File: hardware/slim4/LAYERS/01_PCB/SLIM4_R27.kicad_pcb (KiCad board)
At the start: 6 copper layers, 99.2 x 125 mm, 167 parts, among them J1 FH12A-40S-0.5SH(55), J2 USB4105-GF-A-120, J3 S2B-PH-SM4-TB(LF)(SN), J4 53261-0271, J5 53261-0271, Q1 2N7002, Q2 AO3401A, SW1 D2LS-21, SW2 D2LS-21, SW3 D2LS-21, SW4 D2LS-21, SW5 B3U-1000P, SW6 B3U-1000P, SW7 B3U-1000P, U1 ESP32-P4NRW32X, U10 BQ24074RGTR, U11 TPD2EUSB30DRTR, U12 TPD2EUSB30DRTR, U13 TUSB320LAIRWBR, U14 TPS3808G33DBVR, U2 W25Q512JVEIQ TR, U3 TLV62569DBVR, U4 TPS63070RNMR, U5 TLV75518PDBVR, U6 ME6211C30M5G-N, U7 TPS61165DBVR, U8 MAX98357AETE+T, U9 MAX98357AETE+T, Y1 L327S400H11L

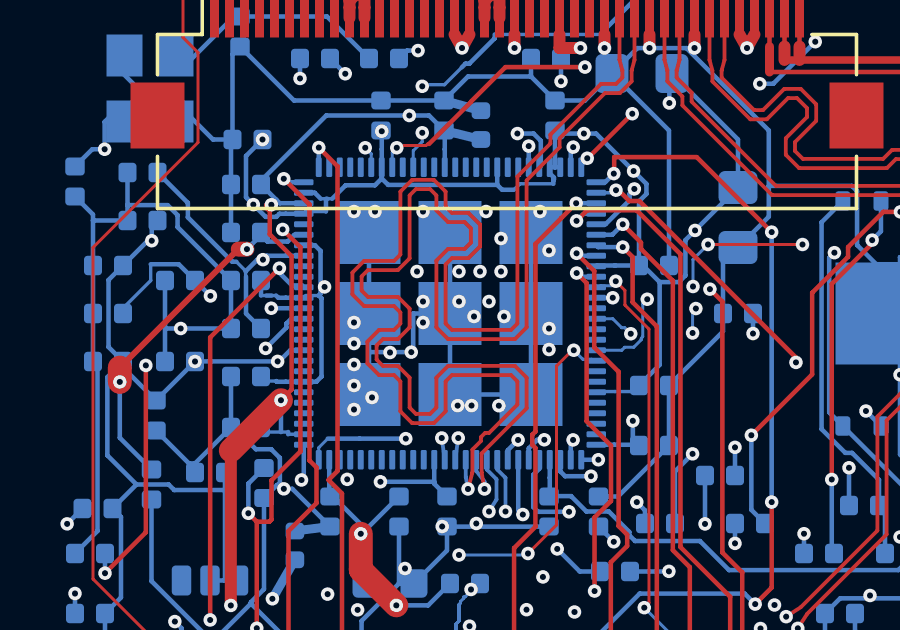
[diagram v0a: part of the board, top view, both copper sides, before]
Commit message: WIP R32: edit 36 puts every new U1 ground via on the exposed pad's copper (31 vias), R27 rebuilt and checks rerun
Co-Authored-By: Claude Opus 5.5 <noreply@anthropic.com>
Claude-Session: https://claude.ai/code/session_01AZXyynf2vqoA1qdTyQFbXM
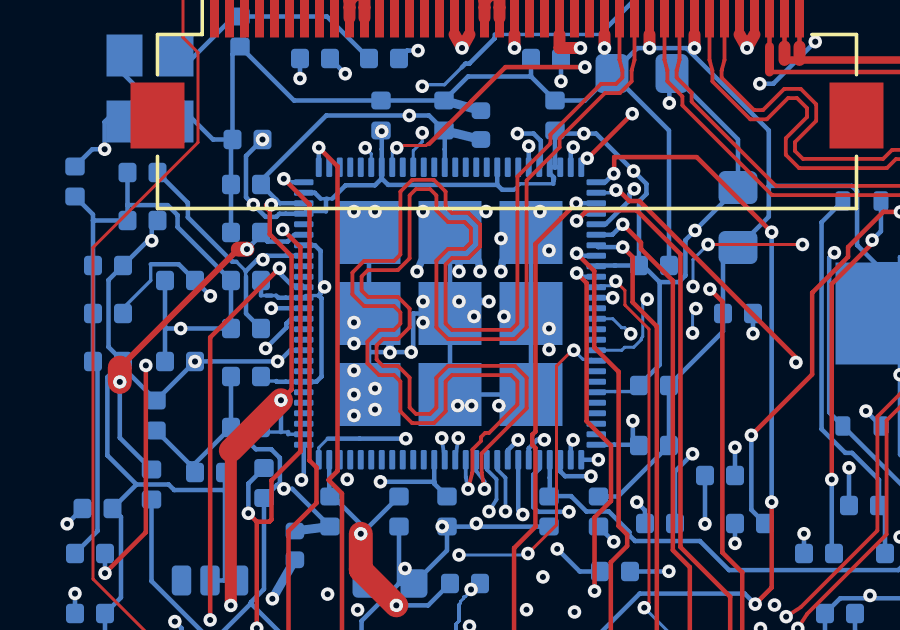
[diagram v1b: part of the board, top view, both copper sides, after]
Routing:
- net GND: track 539.4 -> 542.1 mm, vias 121 -> 122
